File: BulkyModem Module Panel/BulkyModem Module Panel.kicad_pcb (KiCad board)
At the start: 2 copper layers, 100 x 23.2 mm, 15 parts, among them J1 Front Panel, M1 Mounting_Pin, M2 Mounting_Pin, M3 Mounting_Pin, M4 Mounting_Pin, SW1 MODE, SW2 POW

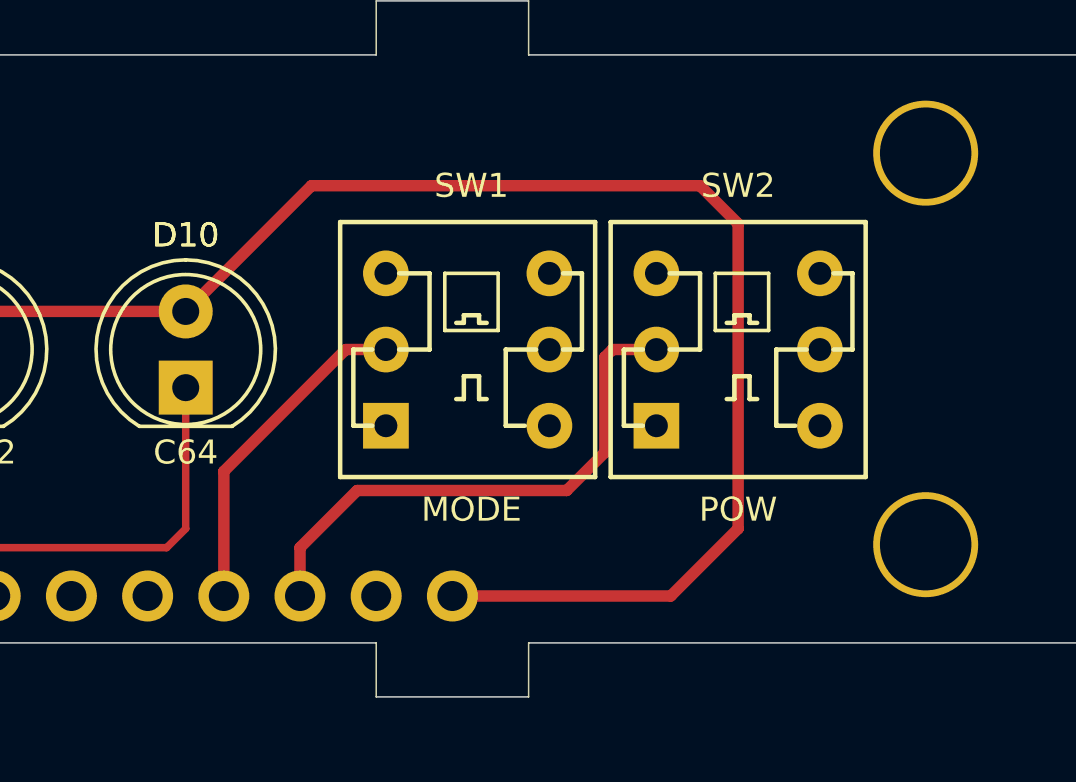
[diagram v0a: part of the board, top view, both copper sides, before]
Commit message: Double up power switch
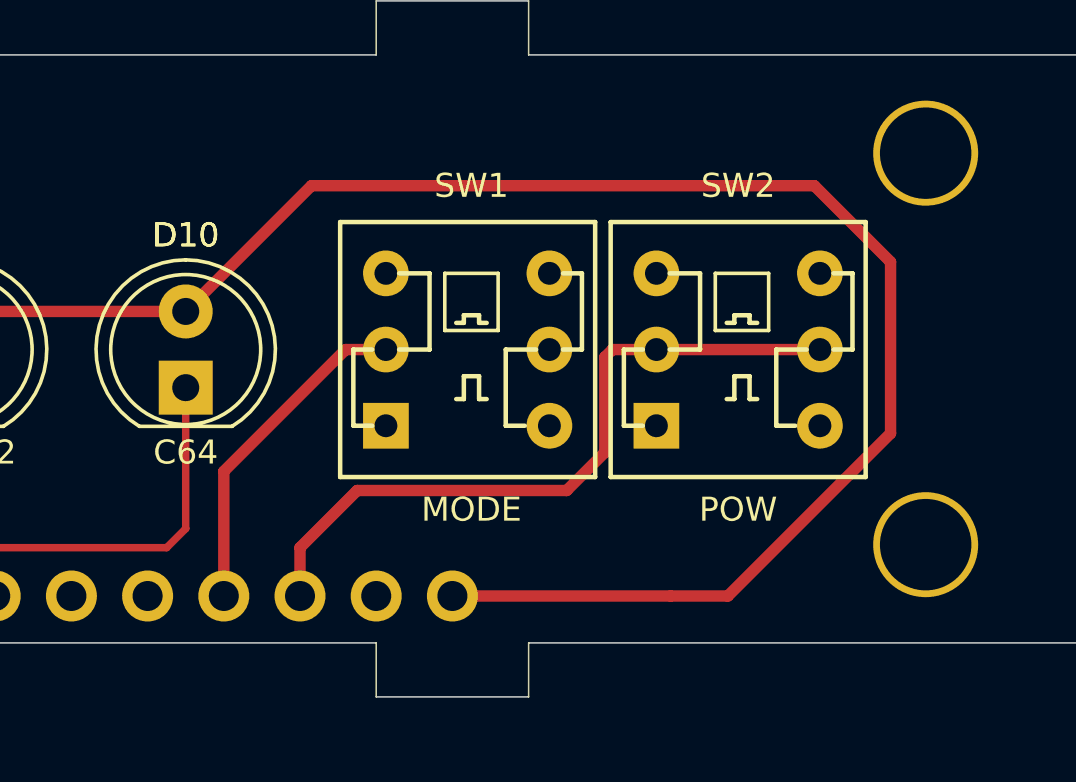
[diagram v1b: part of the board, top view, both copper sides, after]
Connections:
- SW2 pad 5: (no net) -> SW_PWR
- SW2 pad 6: (no net) -> GND
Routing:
- net VCC: track 125.8 -> 133.4 mm
- net SW_PWR: track 18.1 -> 23.5 mm

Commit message: Add DCD
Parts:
- added D1: DCD, LED_THT:LED_D5.0mm, F.Cu at (143.0, 123.9)
- moved D13 4.45 mm to (136.0, 123.9)
- moved D12 3.81 mm to (129.0, 123.9)
- moved D11 1.27 mm to (151.2, 123.9)
- moved D15 1.27 mm to (122.0, 123.9)
- moved D10 0.64 mm to (158.2, 123.9)
- moved D14 0.63 mm to (115.1, 123.9)
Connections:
- J1 pad 10: /LED_C64 -> /LED_RS232
- J1 pad 11: (no net) -> /LED_C64
- J1 pad 5: /LED_RX -> /LED_TX
- J1 pad 6: /LED_TX -> /LED_RX
- J1 pad 7: /LED_CTS -> /LED_RTS
- J1 pad 8: /LED_RTS -> /LED_CTS
- J1 pad 9: /LED_RS232 -> /LED_DCD
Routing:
- net /LED_DCD: track 0.00 -> 13.2 mm
- net /LED_CTS: track 15.7 -> 8.00 mm
- net /LED_RX: track 8.00 -> 12.6 mm
- net /LED_C64: track 25.3 -> 23.0 mm
- net /LED_TX: track 18.9 -> 17.0 mm
- net /LED_RS232: track 20.2 -> 18.9 mm
- net VCC: track 133.4 -> 132.3 mm
- net /LED_RTS: track 7.21 -> 7.73 mm

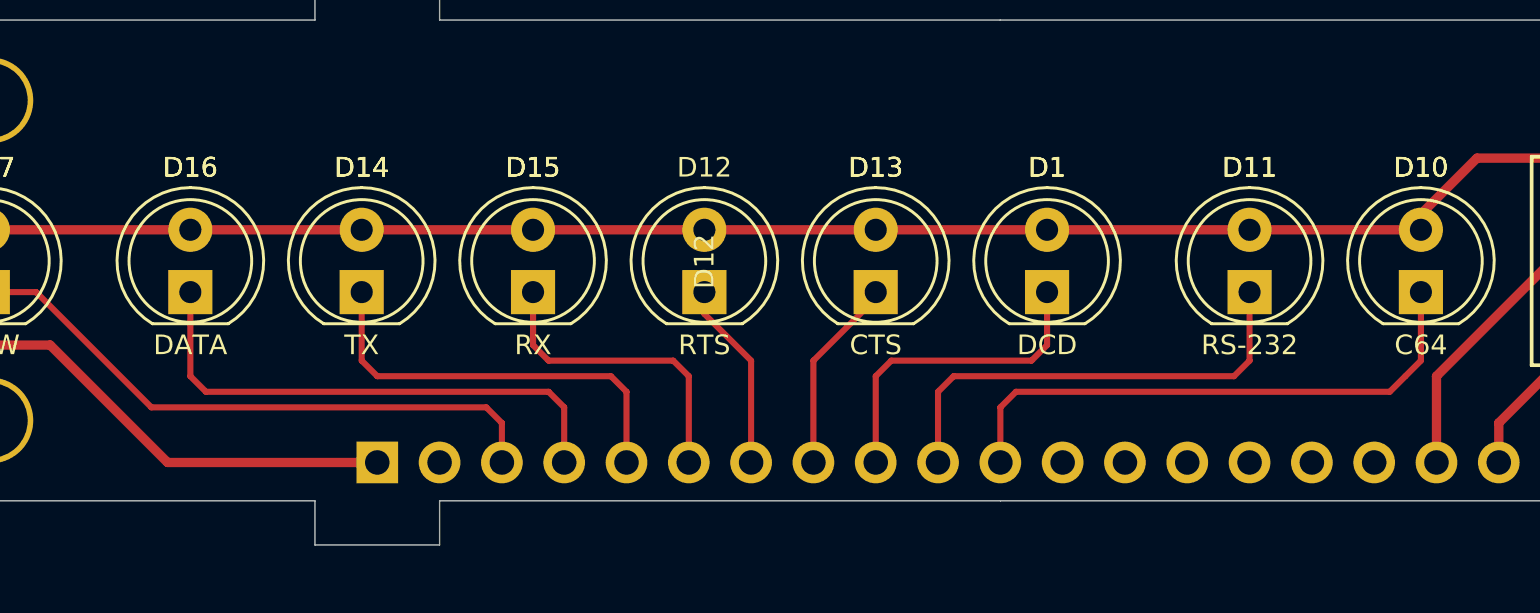
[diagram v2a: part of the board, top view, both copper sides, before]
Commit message: Add RI LED
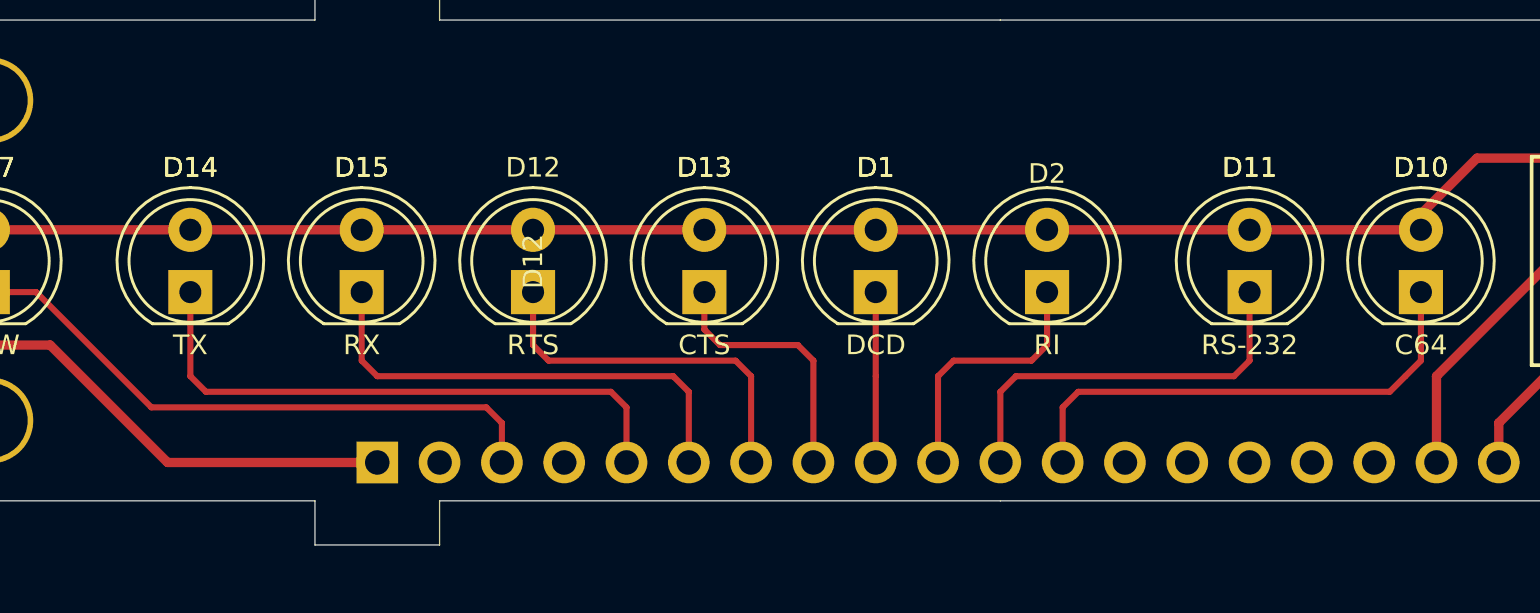
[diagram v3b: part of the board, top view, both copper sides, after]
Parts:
- removed D16: DATA, LED_THT:LED_D5.0mm
- added D2: RI, LED_THT:LED_D5.0mm, F.Cu at (143.0, 123.9)
- moved D1 6.99 mm to (136.0, 123.9)
- moved D14 6.99 mm to (108.1, 123.9)
- moved D12 6.98 mm to (122.0, 123.9)
- moved D15 6.98 mm to (115.1, 123.9)
- moved D13 6.98 mm to (129.0, 123.9)
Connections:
- J1 pad 10: /LED_RS232 -> /LED_RI
- J1 pad 11: /LED_C64 -> /LED_RS232
- J1 pad 12: (no net) -> /LED_C64
- J1 pad 13: (no net) -> Net-(J1-Pad13)
- J1 pad 14: (no net) -> Net-(J1-Pad14)
- J1 pad 15: (no net) -> Net-(J1-Pad15)
- J1 pad 16: (no net) -> Net-(J1-Pad16)
- J1 pad 17: (no net) -> Net-(J1-Pad17)
- J1 pad 4: /LED_DATA -> Net-(J1-Pad4)
- SW1 pad 1: (no net) -> Net-(SW1-Pad1)
- SW1 pad 4: (no net) -> Net-(SW1-Pad4)
- SW1 pad 5: (no net) -> Net-(SW1-Pad5)
- SW1 pad 6: (no net) -> Net-(SW1-Pad6)
- SW2 pad 1: (no net) -> Net-(SW2-Pad1)
- SW2 pad 4: (no net) -> Net-(SW2-Pad4)
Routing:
- net /LED_DATA: track 21.4 -> 0.00 mm
- net /LED_RI: track 0.00 -> 10.6 mm
- net /LED_RTS: track 7.73 -> 15.1 mm
- net /LED_TX: track 17.0 -> 24.0 mm
- net /LED_RX: track 12.6 -> 19.5 mm
- net /LED_DCD: track 13.2 -> 7.20 mm
- net /LED_CTS: track 8.00 -> 10.6 mm
- net /LED_RS232: track 18.9 -> 16.4 mm
- net /LED_C64: track 23.0 -> 20.4 mm
